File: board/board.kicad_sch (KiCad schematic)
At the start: 9 parts, among them J1 Screw_Terminal_01x02, J2 Screw_Terminal_01x03, J3 Screw_Terminal_01x02, U1 ADS1232IPW, U2 TPS7A20xxxDQN

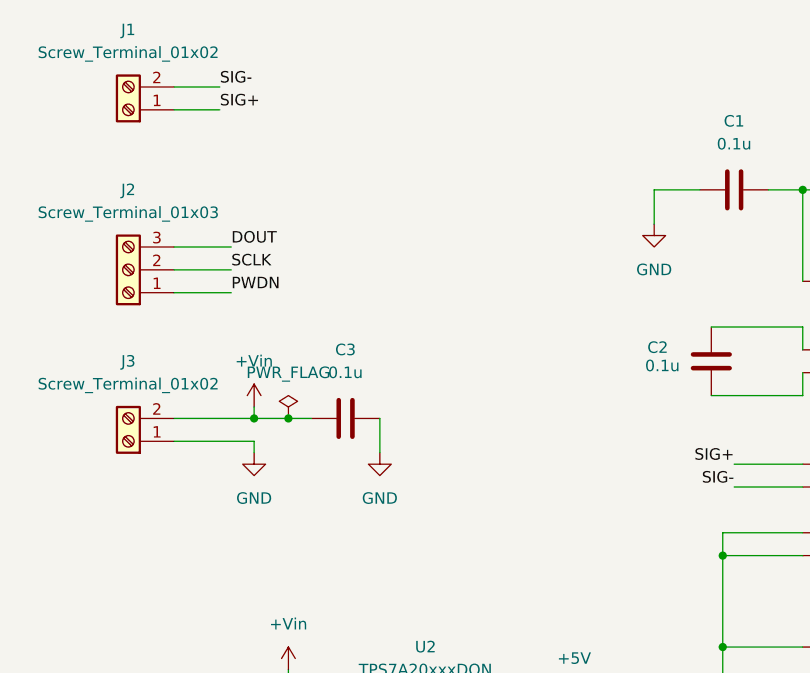
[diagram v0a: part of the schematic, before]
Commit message: terminal for 3.3V line
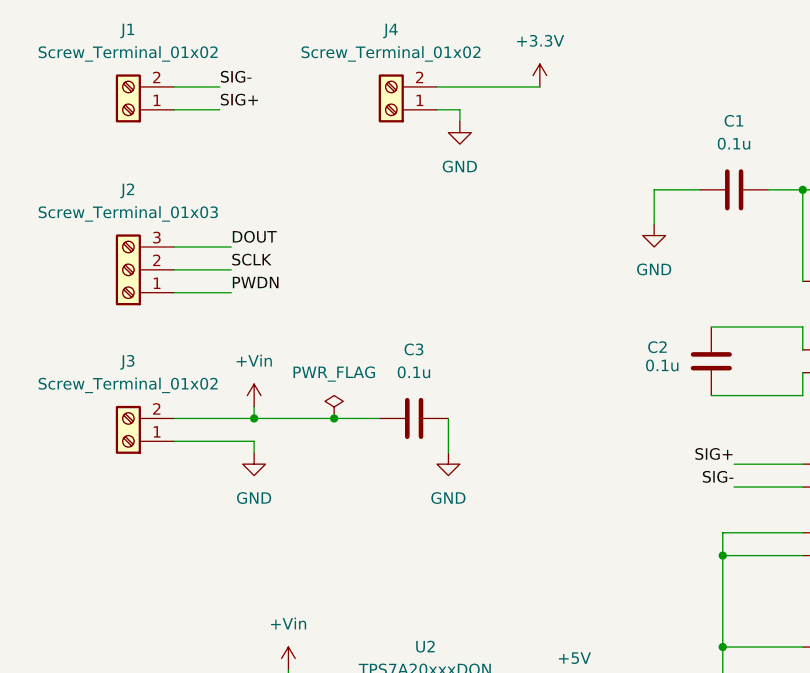
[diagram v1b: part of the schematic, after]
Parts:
- added J4: Screw_Terminal_01x02, symbol Connector:Screw_Terminal_01x02
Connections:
- net +3.3V: now also J4.2 (Pin_2)
- net GND: now also J4.1 (Pin_1)
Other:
- moved on the sheet: C3

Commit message: new design
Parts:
- removed C1: 0.1u, symbol Device:C
- removed J2: Screw_Terminal_01x03, symbol Connector:Screw_Terminal_01x03
- removed U1: ADS1232IPW, symbol Analog_ADC:ADS1232IPW
- removed U2: TPS7A20xxxDQN, Package_SON:Texas_X2SON-4_1x1mm_P0.65mm, symbol Regulator_Linear:TPS7A20xxxDQN
- added C10, C7: 100uF, symbol Device:C
- added C5: 3.3uF, symbol Device:C
- added C6, C8: 10uF, symbol Device:C
- added C9: 15uF, symbol Device:C
- added J2: Screw_Terminal_01x02, symbol Connector:Screw_Terminal_01x02
- added L1: 12uH, symbol Device:L
- added R1: 100k, symbol Device:R_US
- added R2: 5k, symbol Device:R_US
- added R3: 1k, symbol Device:R_US
- added R4: 7k, symbol Device:R_US
- added R5: 200, symbol Device:R_US
- added U1: TPS54202DDC, Package_TO_SOT_SMD:SOT-23-6, symbol Regulator_Switching:TPS54202DDC
- added U2: LM1117DT-5.0, Package_TO_SOT_SMD:TO-252-3_TabPin2, symbol Regulator_Linear:LM1117DT-5.0
- added U3: LM1117DT-ADJ, Package_TO_SOT_SMD:TO-252-3_TabPin2, symbol Regulator_Linear:LM1117DT-ADJ
- added U4: INA333xxDGK, Package_SO:VSSOP-8_3x3mm_P0.65mm, symbol Amplifier_Instrumentation:INA333xxDGK
- C2: value 0.1u -> 100nF
- C3: value 0.1u -> 47pF
- C4: value 0.1u -> 22uF
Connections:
- net SIG+ is gone; now on net GND: J1.1 (Pin_1)
- net +5V: now also C7.2, U2.2 (VO), U4.7 (V+); no longer C4.1
- net GND: now also C4.1, C10.1, C5.1, C6.1, C7.1, C8.1, C9.1, R2.2, R4.2, U1.1 (GND), U2.1 (GND), U4.4 (V-), U4.5 (Ref); no longer C3.1, C4.2
- net at C2.1: now also U1.6 (BOOT)
- net at C2.2: now also L1.1, U1.2 (SW)
- net +3.3V renamed +Vout
- net +Vout: now also U4.6
- net +Vin renamed +10V
- net +10V: now also C10.2, R3.1, U3.2 (VO); no longer C3.2
- net SIG- renamed +24V
- net +24V: now also C5.2, U1.3 (VIN)
- new net: C9.2, R3.2, R4.1, U3.1 (ADJ)
- new net: C3.1, R1.2, R2.1, U1.4 (FB)
- new net: R5.2, U4.1 (Rg)
- new net: R5.1, U4.8 (Rg)
- new net +12V: C3.2, C4.2, C6.2, C8.2, L1.2, R1.1, U2.3 (VI), U3.3 (VI)
- new net +SIG: J2.2 (Pin_2), U4.3 (+)
- new net -SIG: J2.1 (Pin_1), U4.2 (-)
- no-connect marks 2 -> 1
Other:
- note added: "Buck conversion"
- note added: "Input signal voltages"
- note added: "Input supply"
- note added: "LDOs"
- note added: "Op-amp"
- note added: "Output excitation voltages"
- note added: "Output signal"
